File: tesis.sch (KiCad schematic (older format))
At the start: 1 part

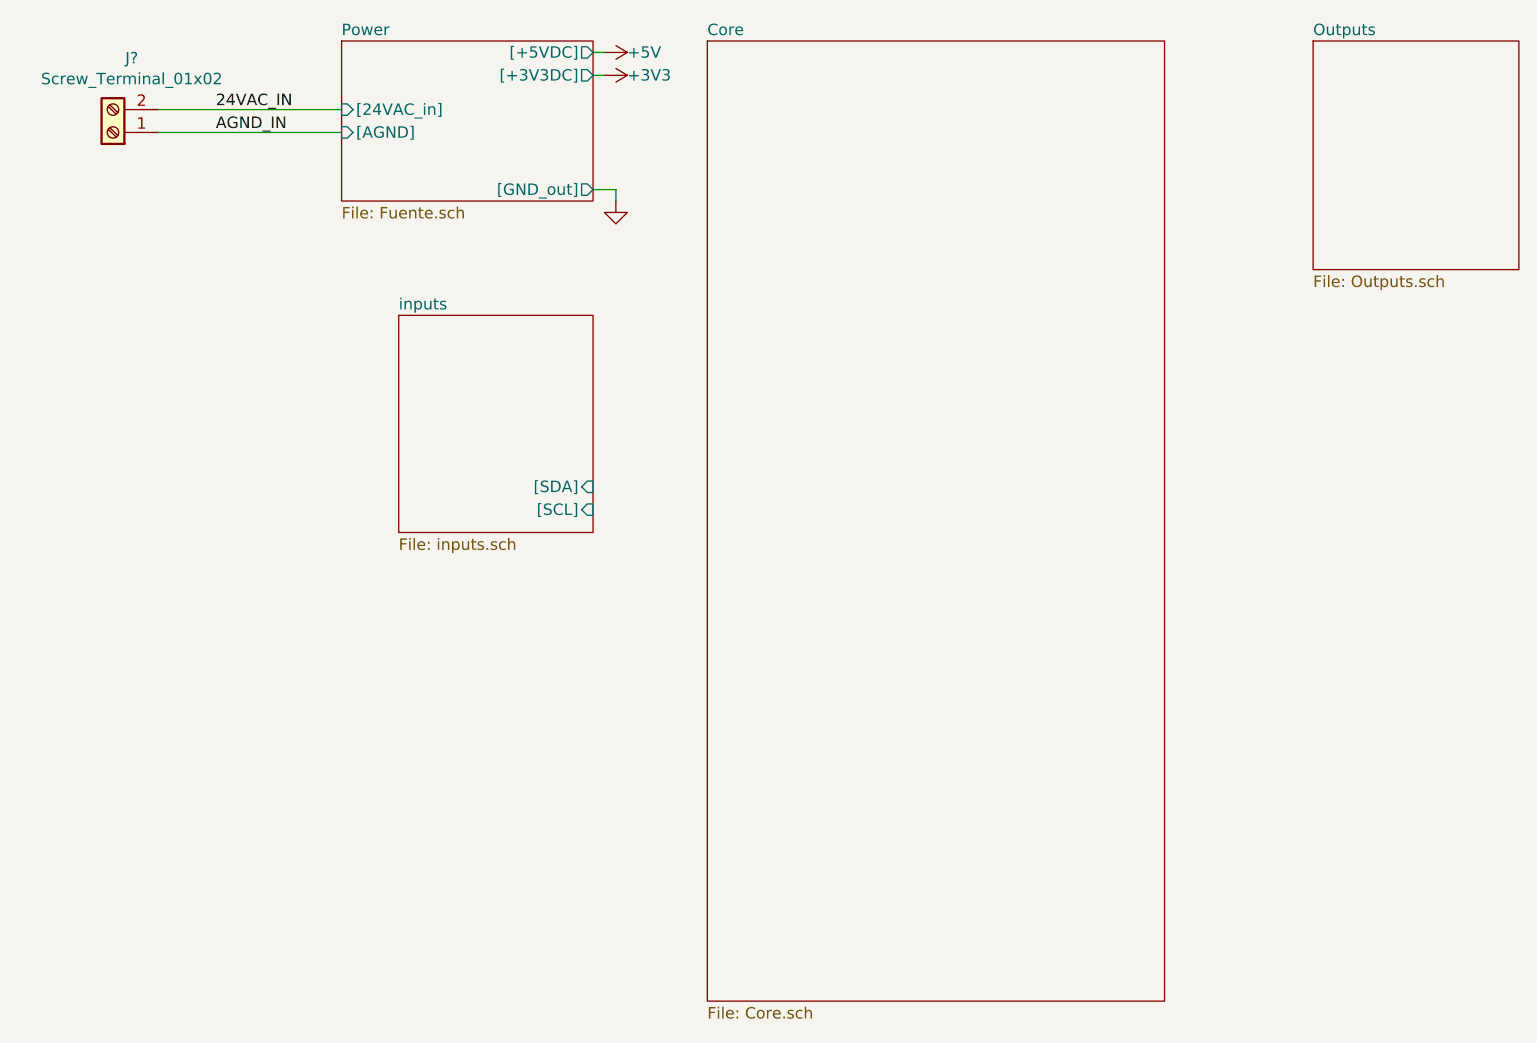
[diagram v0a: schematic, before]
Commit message: Arreglos.
    * Arreglo referencias de address de salida(PCF8574)
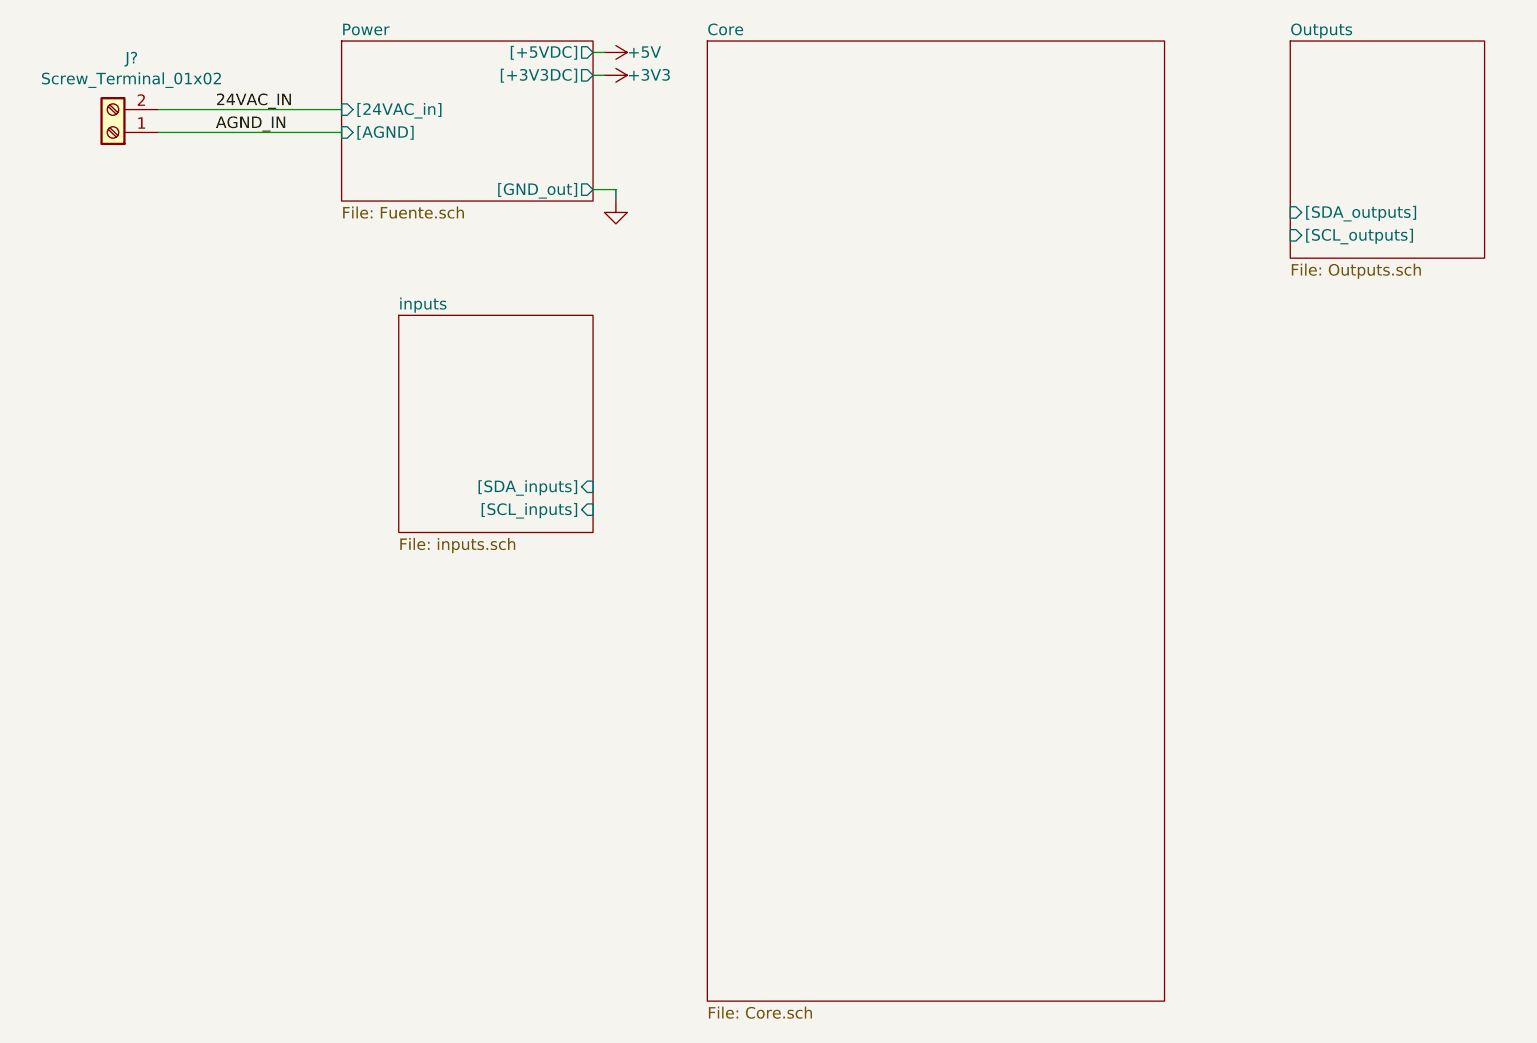
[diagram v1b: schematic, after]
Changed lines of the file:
@@
-$EndSheet
-$Sheet
-S 7350 1450 900  1000
-U 61434A7C
-F0 "Outputs" 50
-F1 "Outputs.sch" 50
 $EndSheet
 $Sheet
@@
 F0 "inputs" 50
 F1 "inputs.sch" 50
-F2 "[SDA]" I R 4200 3400 50
-F3 "[SCL]" I R 4200 3500 50
+F2 "[SCL_inputs]" I R 4200 3500 50
+F3 "[SDA_inputs]" I R 4200 3400 50
 $EndSheet
 $Sheet
@@
 Wire Wire Line
 	2300 1750 3100 1750
+$Sheet
+S 7250 1450 850  950
+U 61434A7C
+F0 "Outputs" 50
+F1 "Outputs.sch" 50
+F2 "[SCL_outputs]" I L 7250 2300 50
+F3 "[SDA_outputs]" I L 7250 2200 50
+$EndSheet
 $EndSCHEMATC
